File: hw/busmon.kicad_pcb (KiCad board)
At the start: 2 copper layers, 24 parts, among them J1 CONN_01X16, J3 DIL14, J4 DIL14, J5 DIL14, J6 DIL14, J7 CONN_01X02, J8 CONN_01X06, Q1 MMBT3906, Q2 MMBT3906, Q3 MMBT3906, Q4 MMBT3906, U1 ATMEGA164A-A

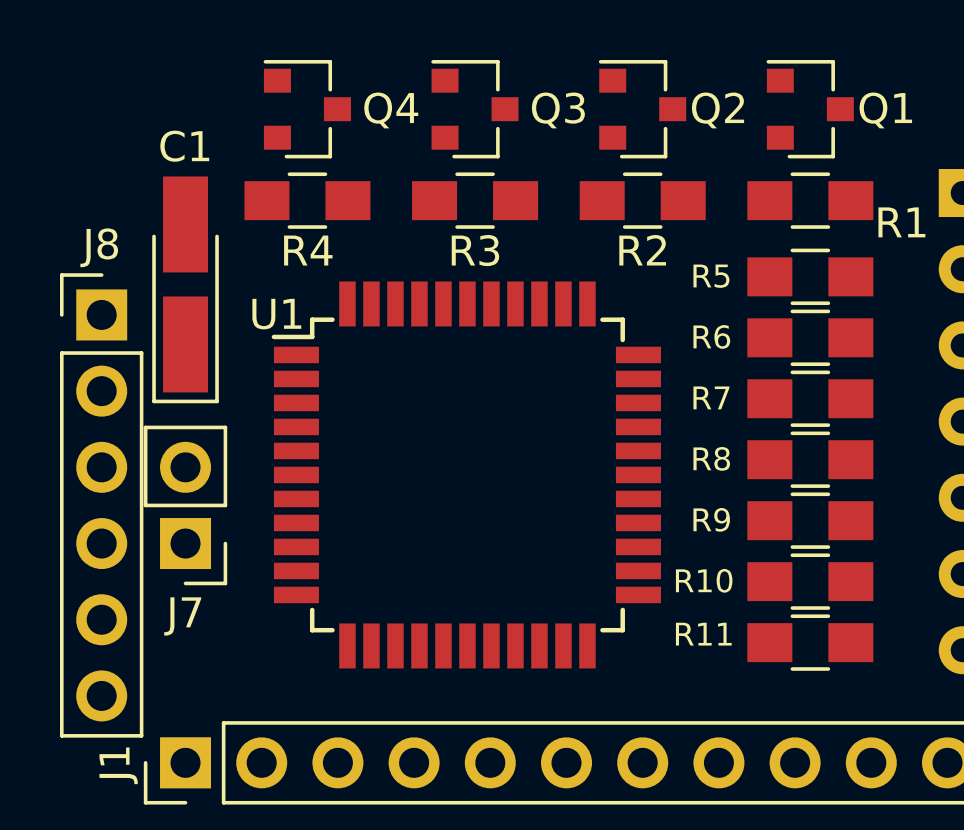
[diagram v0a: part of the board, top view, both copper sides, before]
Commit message: started routing power connections
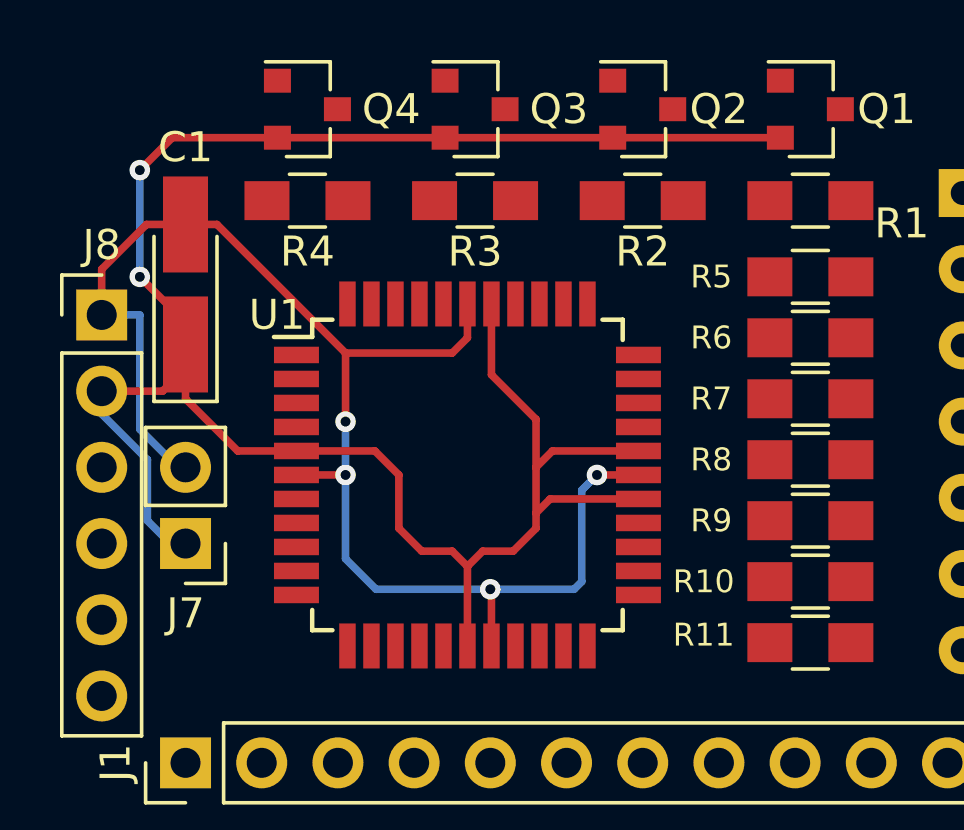
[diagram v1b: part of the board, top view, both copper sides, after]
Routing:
- net VCC: track 0.00 -> 74.1 mm, vias 0 -> 2
- net GND: track 0.00 -> 48.5 mm, vias 0 -> 4
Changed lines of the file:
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@@
   (general
     (links 91)
-    (no_connects 91)
-    (area 83.077267 79.352599 157.467401 108.128734)
+    (no_connects 74)
+    (area 84.347267 79.352599 157.467401 108.128734)
     (thickness 1.6)
     (drawings 0)
-    (tracks 0)
+    (tracks 69)
     (zones 0)
     (modules 24)
@@
   )
   (setup
-    (last_trace_width 0.1524)
+    (last_trace_width 0.254)
+    (user_trace_width 0.254)
     (trace_clearance 0.1524)
     (zone_clearance 0.508)
@@
     )
   )
+  (segment (start 106.442 82.23) (end 112.03 82.23) (width 0.254) (layer F.Cu) (net 1) (status C00000))
+  (segment (start 100.854 82.23) (end 106.442 82.23) (width 0.254) (layer F.Cu) (net 1) (status C00000))
+  (segment (start 95.266 82.23) (end 100.854 82.23) (width 0.254) (layer F.Cu) (net 1) (status C00000))
+  (segment (start 92.202 89.122) (end 92.202 88.392) (width 0.254) (layer F.Cu) (net 1) (status C00000))
+  (segment (start 92.202 88.392) (end 90.678 86.868) (width 0.254) (layer F.Cu) (net 1) (status 400000))
+  (segment (start 91.76 82.23) (end 95.266 82.23) (width 0.254) (layer F.Cu) (net 1) (status 800000))
+  (segment (start 90.678 83.312) (end 91.76 82.23) (width 0.254) (layer F.Cu) (net 1))
+  (via (at 90.678 83.312) (size 0.6858) (drill 0.3302) (layers F.Cu B.Cu) (net 1))
+  (segment (start 90.678 86.868) (end 90.678 83.312) (width 0.254) (layer B.Cu) (net 1))
+  (via (at 90.678 86.868) (size 0.6858) (drill 0.3302) (layers F.Cu B.Cu) (net 1))
+  (segment (start 102.4 87.772) (end 102.4 90.132) (width 0.254) (layer F.Cu) (net 1))
+  (segment (start 103.886 91.618) (end 103.886 93.218) (width 0.254) (layer F.Cu) (net 1))
+  (segment (start 102.4 90.132) (end 103.886 91.618) (width 0.254) (layer F.Cu) (net 1))
+  (segment (start 107.3 92.672) (end 104.432 92.672) (width 0.254) (layer F.Cu) (net 1))
+  (segment (start 103.886 93.218) (end 103.886 94.742) (width 0.254) (layer F.Cu) (net 1))
+  (segment (start 104.432 92.672) (end 103.886 93.218) (width 0.254) (layer F.Cu) (net 1))
+  (segment (start 107.3 94.272) (end 104.356 94.272) (width 0.254) (layer F.Cu) (net 1))
+  (segment (start 102.108 96.012) (end 101.6 96.52) (width 0.254) (layer F.Cu) (net 1))
+  (segment (start 103.124 96.012) (end 102.108 96.012) (width 0.254) (layer F.Cu) (net 1))
+  (segment (start 103.886 95.25) (end 103.124 96.012) (width 0.254) (layer F.Cu) (net 1))
+  (segment (start 103.886 94.742) (end 103.886 95.25) (width 0.254) (layer F.Cu) (net 1))
+  (segment (start 104.356 94.272) (end 103.886 94.742) (width 0.254) (layer F.Cu) (net 1))
+  (segment (start 95.9 92.672) (end 98.514 92.672) (width 0.254) (layer F.Cu) (net 1))
+  (segment (start 101.6 96.52) (end 101.6 99.172) (width 0.254) (layer F.Cu) (net 1))
+  (segment (start 101.092 96.012) (end 101.6 96.52) (width 0.254) (layer F.Cu) (net 1))
+  (segment (start 100.076 96.012) (end 101.092 96.012) (width 0.254) (layer F.Cu) (net 1))
+  (segment (start 99.314 95.25) (end 100.076 96.012) (width 0.254) (layer F.Cu) (net 1))
+  (segment (start 99.314 93.472) (end 99.314 95.25) (width 0.254) (layer F.Cu) (net 1))
+  (segment (start 98.514 92.672) (end 99.314 93.472) (width 0.254) (layer F.Cu) (net 1))
+  (segment (start 92.202 89.122) (end 92.202 90.932) (width 0.254) (layer F.Cu) (net 1))
+  (segment (start 93.942 92.672) (end 95.9 92.672) (width 0.254) (layer F.Cu) (net 1))
+  (segment (start 92.202 90.932) (end 93.942 92.672) (width 0.254) (layer F.Cu) (net 1))
+  (segment (start 92.202 95.758) (end 91.694 95.758) (width 0.254) (layer B.Cu) (net 1))
+  (segment (start 91.694 95.758) (end 90.932 94.996) (width 0.254) (layer B.Cu) (net 1))
+  (segment (start 90.932 94.996) (end 90.932 92.964) (width 0.254) (layer B.Cu) (net 1))
+  (segment (start 90.932 92.964) (end 89.408 91.44) (width 0.254) (layer B.Cu) (net 1))
+  (segment (start 89.408 91.44) (end 89.408 90.678) (width 0.254) (layer B.Cu) (net 1))
+  (segment (start 92.202 89.122) (end 92.202 89.916) (width 0.254) (layer F.Cu) (net 1))
+  (segment (start 92.202 89.916) (end 91.44 90.678) (width 0.254) (layer F.Cu) (net 1))
+  (segment (start 91.44 90.678) (end 89.408 90.678) (width 0.254) (layer F.Cu) (net 1))
+  (segment (start 107.3 93.472) (end 105.918 93.472) (width 0.254) (layer F.Cu) (net 2))
+  (segment (start 105.156 97.282) (end 102.362 97.282) (width 0.254) (layer B.Cu) (net 2))
+  (segment (start 105.41 97.028) (end 105.156 97.282) (width 0.254) (layer B.Cu) (net 2))
+  (segment (start 105.41 93.98) (end 105.41 97.028) (width 0.254) (layer B.Cu) (net 2))
+  (segment (start 105.918 93.472) (end 105.41 93.98) (width 0.254) (layer B.Cu) (net 2))
+  (via (at 105.918 93.472) (size 0.6858) (drill 0.3302) (layers F.Cu B.Cu) (net 2))
+  (segment (start 97.536 93.472) (end 97.536 96.266) (width 0.254) (layer B.Cu) (net 2))
+  (segment (start 102.4 97.32) (end 102.4 99.172) (width 0.254) (layer F.Cu) (net 2))
+  (segment (start 102.362 97.282) (end 102.4 97.32) (width 0.254) (layer F.Cu) (net 2))
+  (via (at 102.362 97.282) (size 0.6858) (drill 0.3302) (layers F.Cu B.Cu) (net 2))
+  (segment (start 98.552 97.282) (end 102.362 97.282) (width 0.254) (layer B.Cu) (net 2))
+  (segment (start 97.536 96.266) (end 98.552 97.282) (width 0.254) (layer B.Cu) (net 2))
+  (segment (start 97.536 89.408) (end 97.536 91.694) (width 0.254) (layer F.Cu) (net 2))
+  (segment (start 97.536 93.472) (end 95.9 93.472) (width 0.254) (layer F.Cu) (net 2))
+  (via (at 97.536 93.472) (size 0.6858) (drill 0.3302) (layers F.Cu B.Cu) (net 2))
+  (segment (start 97.536 91.694) (end 97.536 93.472) (width 0.254) (layer B.Cu) (net 2))
+  (via (at 97.536 91.694) (size 0.6858) (drill 0.3302) (layers F.Cu B.Cu) (net 2))
+  (segment (start 92.202 85.122) (end 93.25 85.122) (width 0.254) (layer F.Cu) (net 2))
+  (segment (start 101.6 88.9) (end 101.6 87.772) (width 0.254) (layer F.Cu) (net 2))
+  (segment (start 101.092 89.408) (end 101.6 88.9) (width 0.254) (layer F.Cu) (net 2))
+  (segment (start 97.536 89.408) (end 101.092 89.408) (width 0.254) (layer F.Cu) (net 2))
+  (segment (start 93.25 85.122) (end 97.536 89.408) (width 0.254) (layer F.Cu) (net 2))
+  (segment (start 92.202 85.122) (end 90.9 85.122) (width 0.254) (layer F.Cu) (net 2))
+  (segment (start 89.408 86.614) (end 89.408 88.138) (width 0.254) (layer F.Cu) (net 2))
+  (segment (start 90.9 85.122) (end 89.408 86.614) (width 0.254) (layer F.Cu) (net 2))
+  (segment (start 90.678 88.138) (end 89.408 88.138) (width 0.254) (layer B.Cu) (net 2))
+  (segment (start 92.202 93.218) (end 91.948 93.218) (width 0.254) (layer B.Cu) (net 2))
+  (segment (start 91.948 93.218) (end 90.678 91.948) (width 0.254) (layer B.Cu) (net 2))
+  (segment (start 90.678 91.948) (end 90.678 88.138) (width 0.254) (layer B.Cu) (net 2))
 )

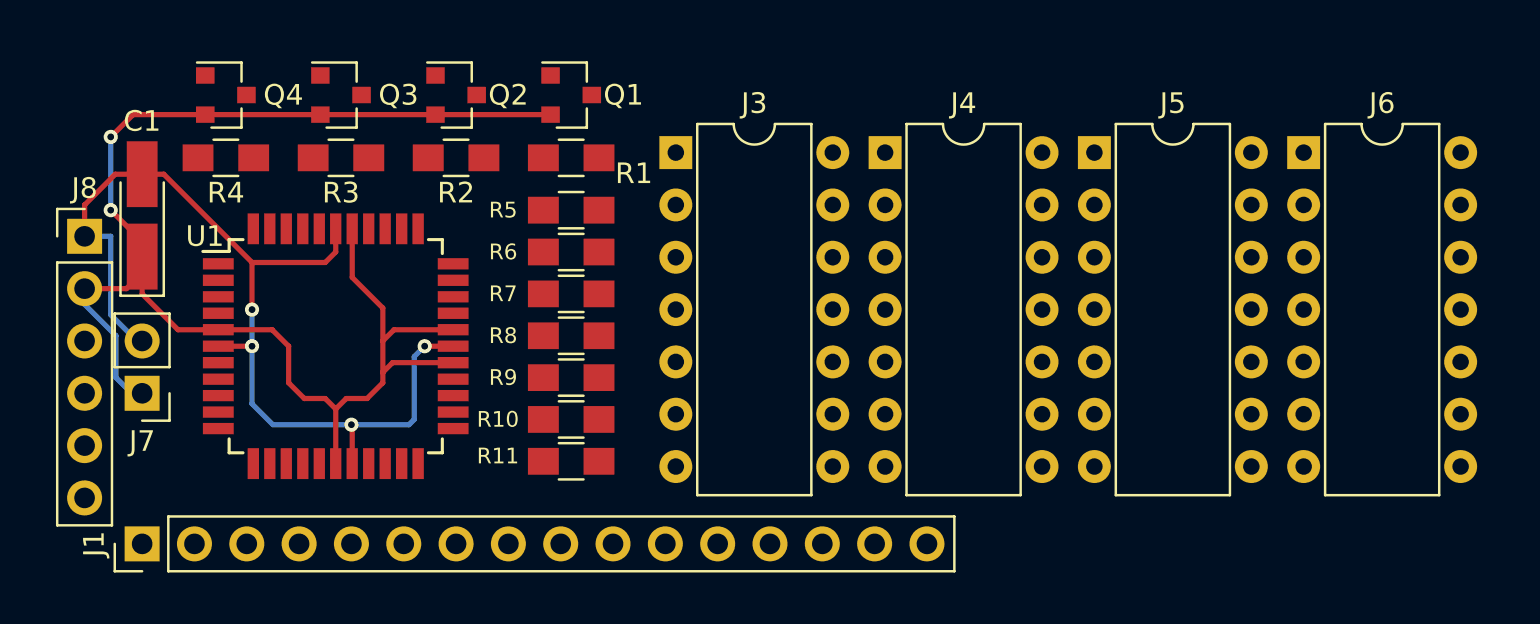
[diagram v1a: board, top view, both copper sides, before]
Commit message: routing more signals
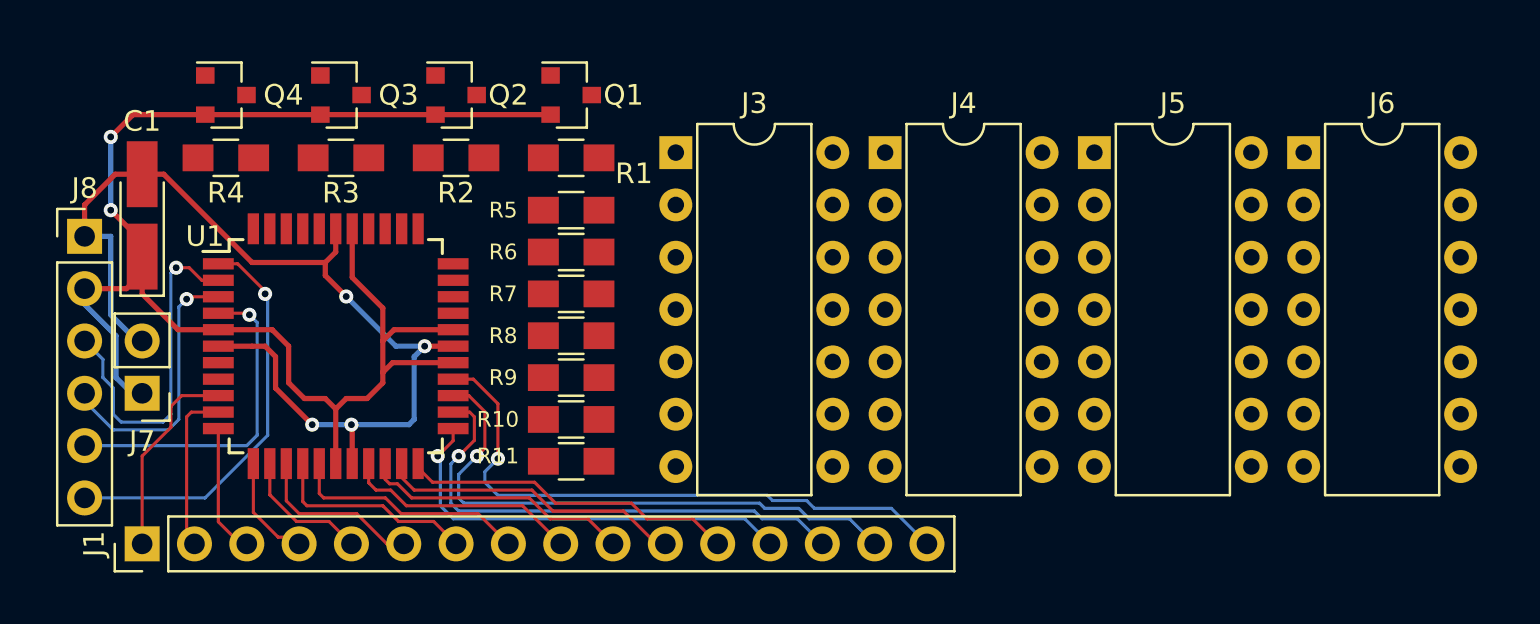
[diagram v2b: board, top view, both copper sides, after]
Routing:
- net /D15: track 0.00 -> 29.4 mm, vias 0 -> 1
- net /D14: track 0.00 -> 27.7 mm, vias 0 -> 1
- net /D13: track 0.00 -> 24.6 mm, vias 0 -> 1
- net /D12: track 0.00 -> 20.9 mm, vias 0 -> 1
- net Net-(J8-Pad6): track 0.00 -> 20.0 mm, vias 0 -> 1
- net Net-(J8-Pad3): track 0.00 -> 16.8 mm, vias 0 -> 1
- net /D11: track 0.00 -> 16.3 mm
- net /-RST: track 0.00 -> 16.1 mm, vias 0 -> 1
- net /D10: track 0.00 -> 14.8 mm
- net Net-(J8-Pad4): track 0.00 -> 13.3 mm, vias 0 -> 1
- net /D9: track 0.00 -> 13.1 mm
- net /D7: track 0.00 -> 11.6 mm
- net /D8: track 0.00 -> 11.5 mm
- net /D6: track 0.00 -> 10.1 mm
- net /D0: track 0.00 -> 9.77 mm
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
